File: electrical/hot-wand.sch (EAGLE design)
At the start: 203 parts, among them IC1 12V R-78K12-2.0, IC2 3V3 R-78K3.3, Q1 STP19NF20, Q2 IRF510, Q3 BC846B, Q4 SIS862ADN-T1-GE3, Q5 SIS862ADN-T1-GE3, Q6 DMTH64M2LPDWQ-13, Q7 SIS862ADN-T1-GE3, Q8 2N7002K, Q9 G3404, SW1 SW-TACT-SIDE, U1 TPS54560DDA, U2 1EDN8511BXUSA1, U3 STM32F030F4P6, U4 SSD1306-4PIN-0.91N-VERT, U5 INA138, U6 LM74810QDRRRQ1, U7 AP53781, Y1 27.12 MHz 10pF

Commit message: part num update
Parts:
- U3: value STM32F030F4P6 -> STM32F042F6P6
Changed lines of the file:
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@@
 <attribute name="JLC-DNP" value="1"/>
 </part>
-<part name="U3" library="hot-wand" deviceset="STM32F030F4P6" device="">
+<part name="U3" library="hot-wand" deviceset="STM32F030F4P6" device="" value="STM32F042F6P6">
 <attribute name="JLCPARTNUM" value="C2969989"/>
 <attribute name="JLC_ROTATION" value="180"/>

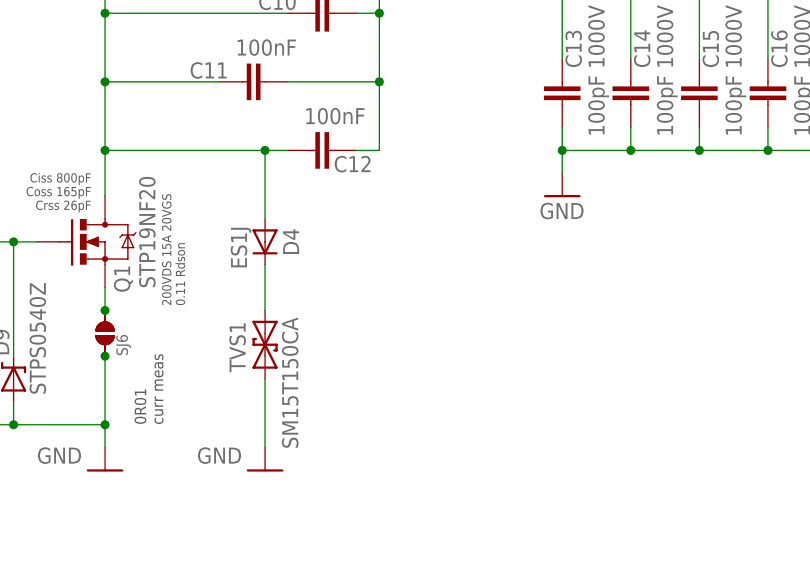
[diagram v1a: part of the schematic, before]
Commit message: lower voltage input limit for lite design
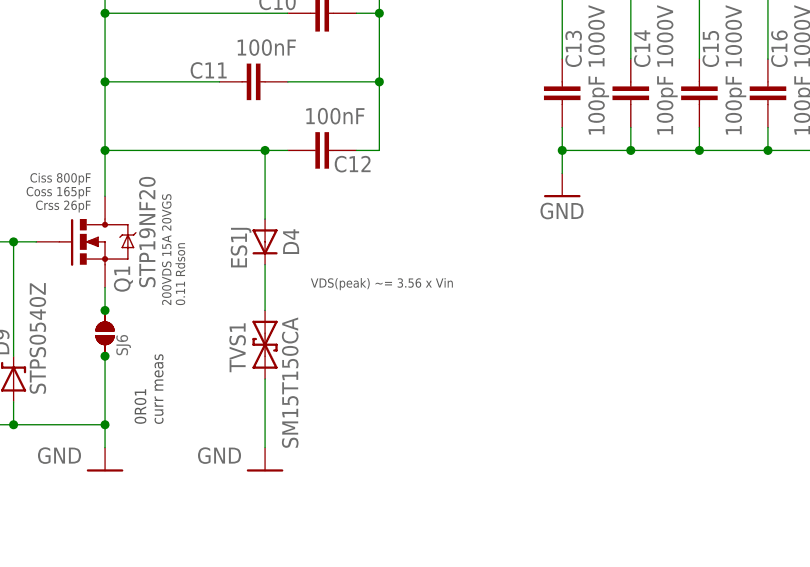
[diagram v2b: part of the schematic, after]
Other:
- note added: "VDS(peak) ~= 3.56 x Vin"
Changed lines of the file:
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@@
 from high battery voltage</text>
 <text x="130.556" y="-596.138" size="1.016" layer="97">50V each</text>
+<text x="81.28" y="-177.8" size="1.016" layer="97">VDS(peak) ~= 3.56 x Vin</text>
 </plain>
 <instances>

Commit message: capacitor footprint improvements
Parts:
- removed FAN2: FAN-TIEDOWN-20MM-V1, hot-wand:FAN-TIEDOWN-20MM-V1
- C2, C4: device hot-wand:CAP_POLPTH4 -> hot-wand:CAP_POLPTH5
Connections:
- net GND: no longer FAN2.1
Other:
- note removed: "MS2006H12D-RSR"
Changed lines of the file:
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@@
 <attribute name="JLCPARTNUM" value="C1613"/>
 </part>
-<part name="C2" library="hot-wand" deviceset="CAP_POL" device="PTH4" value="100uF 50V">
+<part name="C2" library="hot-wand" deviceset="CAP_POL" device="PTH5" value="100uF 50V">
 <attribute name="JLC-DNP" value="1"/>
 <attribute name="PARTNUM" value="EEU-FR1H101B;EEU-FR1J101B"/>
@@
 <attribute name="JLCPARTNUM" value="C21190"/>
 </part>
-<part name="C4" library="hot-wand" deviceset="CAP_POL" device="PTH4" value="100uF 50V">
+<part name="C4" library="hot-wand" deviceset="CAP_POL" device="PTH5" value="100uF 50V">
 <attribute name="JLC-DNP" value="1"/>
 </part>
@@
 <attribute name="PARTNUM" value="MLASU31LBB5106KTNA01;GRT31CR61H106KE01K"/>
 </part>
-<part name="FAN2" library="hot-wand" deviceset="FAN-TIEDOWN" device="-20MM-V1" value="FAN-TIEDOWN-20MM-V1">
-<attribute name="JLC-DNP" value="1"/>
-<attribute name="PARTNUM" value="MS2006H12D-RSR"/>
-</part>
 <part name="PCB2" library="hot-wand" deviceset="PCB-ART-VERSION" device="">
 <attribute name="JLC-DNP" value="1"/>
@@
 <part name="GND61" library="hot-wand" deviceset="GND" device=""/>
 <part name="GND1" library="hot-wand" deviceset="GND" device=""/>
-<part name="GND62" library="hot-wand" deviceset="GND" device=""/>
 <part name="SJ8" library="hot-wand" deviceset="SJ-SMALL" device="-1206-SJ"/>
 <part name="SJ6" library="hot-wand" deviceset="SJ-SMALL" device="-1206-SJ"/>
@@
 <text x="121.158" y="-34.036" size="0.8128" layer="97" rot="R180" align="top-left">FB target 0.8V</text>
 <text x="161.798" y="-14.478" size="0.6096" layer="97" rot="R180" align="top-left">calculations say 13uH minimum</text>
-<text x="289.56" y="-415.544" size="0.8128" layer="97" rot="R180" align="top-left">MS2006H12D-RSR</text>
 <text x="312.42" y="-472.44" size="5.08" layer="97">Fan CTRL</text>
 <text x="312.42" y="-474.98" size="1.778" layer="97">(optional)</text>
@@
 <attribute name="JLCPARTNUM" x="337.82" y="-408.94" size="1.778" layer="96" rot="R270" display="off"/>
 </instance>
-<instance part="FAN2" gate="A" x="271.78" y="-426.72" smashed="yes">
-<attribute name="NAME" x="271.78" y="-429.26" size="1.778" layer="95"/>
-</instance>
 <instance part="PCB2" gate="A" x="322.58" y="-25.4"/>
 <instance part="Q9" gate="G$1" x="327.66" y="-447.04" smashed="yes">
@@
 <attribute name="VALUE" x="307.34" y="-27.94" size="1.778" layer="96"/>
 </instance>
-<instance part="GND62" gate="1" x="292.1" y="-421.64"/>
 <instance part="SJ8" gate="A" x="35.56" y="-223.52"/>
 <instance part="SJ6" gate="A" x="58.42" y="-182.88" rot="R90"/>
@@
 </segment>
 <segment>
-<pinref part="FAN2" gate="A" pin="1"/>
-<pinref part="GND62" gate="1" pin="GND"/>
-</segment>
-<segment>

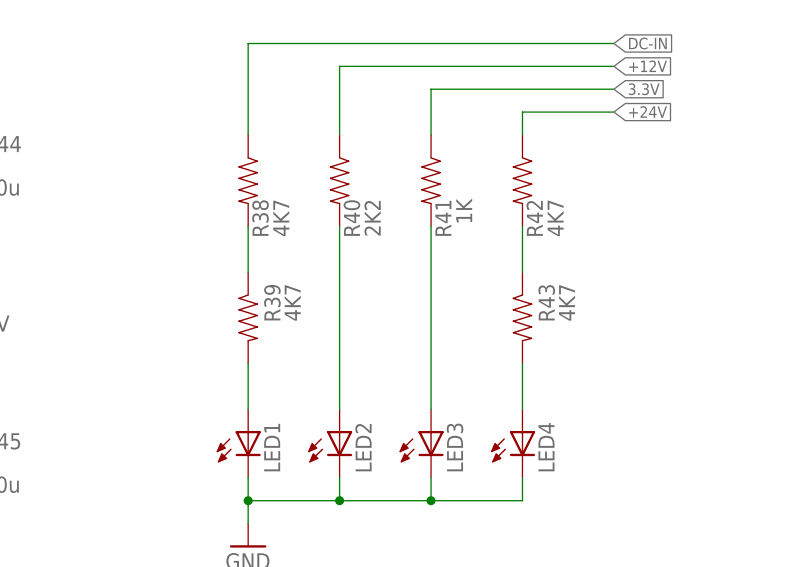
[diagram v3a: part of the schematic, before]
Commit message: inductor pin spacing, capacitor footprint silk, LED resistor changes
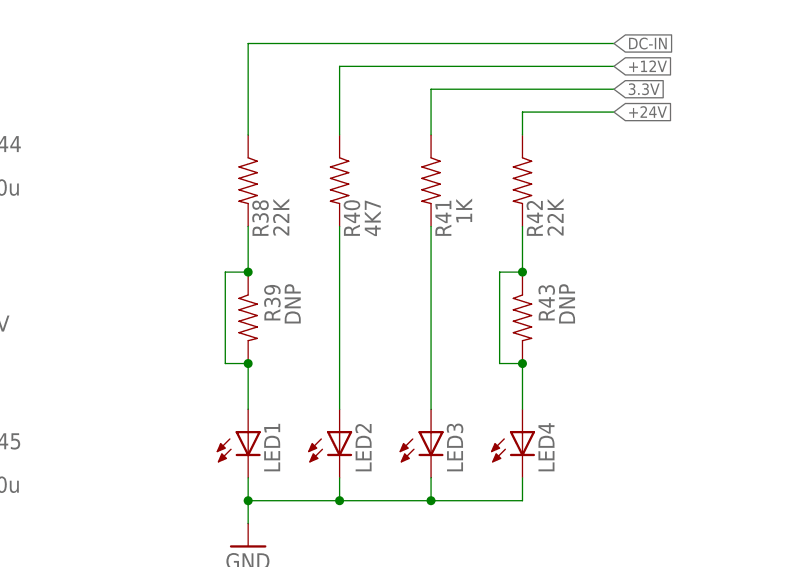
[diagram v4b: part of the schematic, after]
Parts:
- L1: device hot-wand:INDUCTORRADIAL_D12.7_P6.35 -> hot-wand:INDUCTORRADIAL_D12.7_COMBO
- R38, R42: value 4K7 -> 22K; JLCPARTNUM C23162 -> C31850
- R39, R43: value 4K7 -> DNP; DNP (none) -> 1; JLCPARTNUM C23162 -> (none)
- R40: value 2K2 -> 4K7; JLCPARTNUM C4190 -> C23162
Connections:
- removed net N$46: LED1.A, R39.2
- removed net N$64: LED4.A, R43.2
- net N$49: now also LED1.A, R39.2
- net N$62: now also LED4.A, R43.2

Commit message: corrected pot direction
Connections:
- net 3.3V: now also VR2.E; no longer VR2.A
- net BUCK-FB: now also VR1.A; no longer VR1.E
- net N$25: now also VR1.E; no longer VR1.A
- net N$45: now also VR2.A; no longer VR2.E
- net N$50: now also VR4.E; no longer VR4.A
- net N$56: now also VR3.E; no longer VR3.A
- net N$8: now also VR3.A; no longer VR3.E
- net RF-FB-RECTIFIED: now also VR4.A; no longer VR4.E
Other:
- moved on the sheet: VR1, VR4

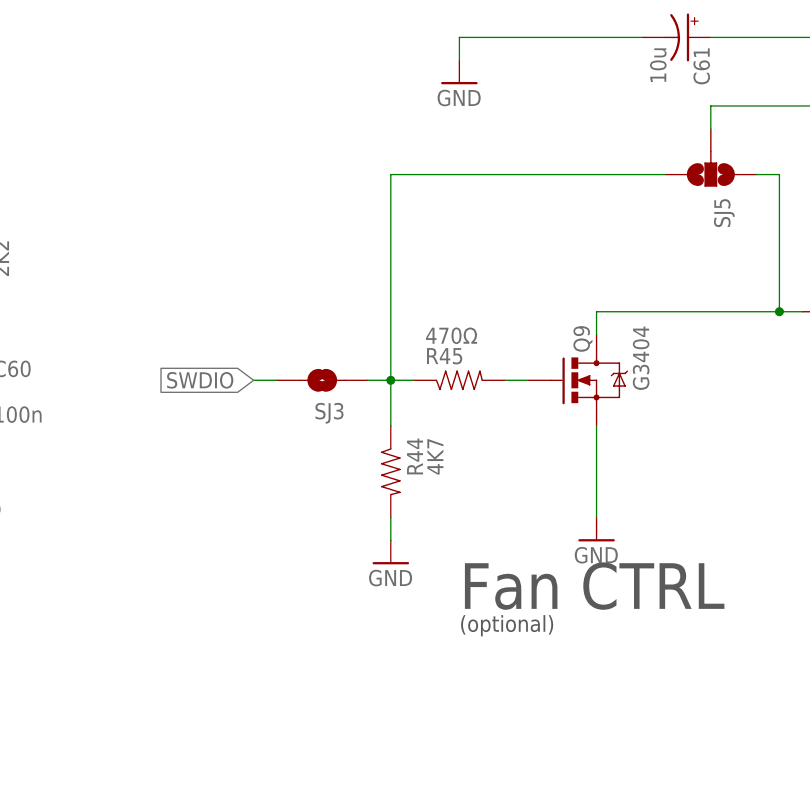
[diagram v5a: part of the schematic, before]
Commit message: renamed nets
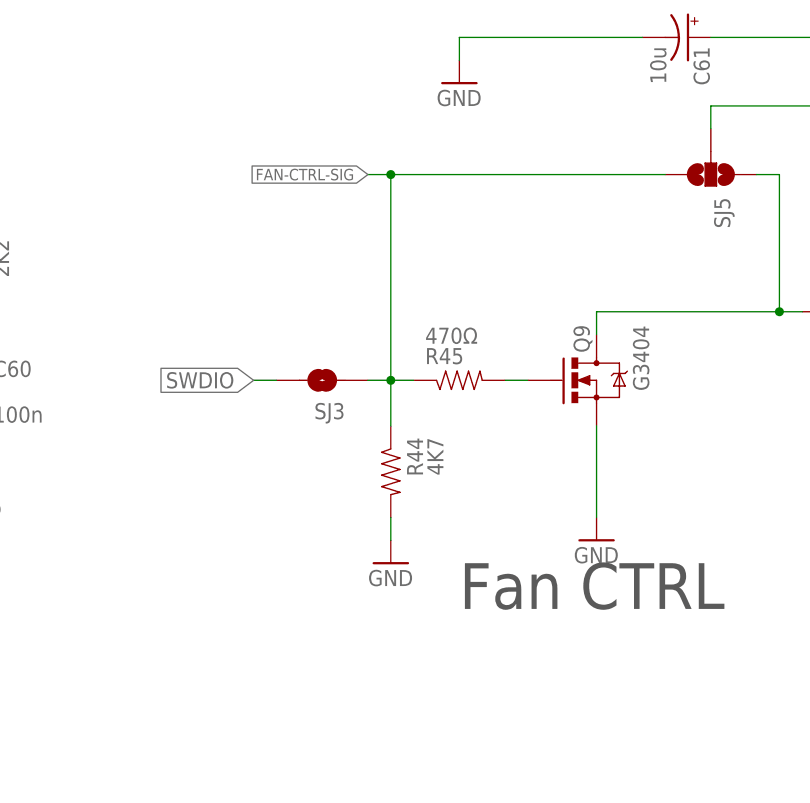
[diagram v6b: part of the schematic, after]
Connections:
- net N$12 renamed RF-FINAL
- net N$13 renamed Q1-VD
- net N$18 renamed Q2-VD
- net N$23 renamed BUCK-SWITCH-NODE
- net N$24 renamed BUCK-1ST-STAGE
- net N$26 renamed MCU-BOOT0
- net N$31 renamed VIN-XT30
- net N$32 renamed U6-EN
- net N$33 renamed MCU-OSC-OUT
- net N$34 renamed MCU-OSC-IN
- net N$36 renamed U7-VGA
- net N$37 renamed U7-VGA-2
- net N$39 renamed USB-VBUS
- net N$41 renamed USB-CC2
- net N$42 renamed U7-VSEL
- net N$44 renamed USB-CC1
- net N$51 renamed FAN-CTRL-SIG
- net N$52 renamed Q9-VD
- net N$54 renamed U7-ISEL
- net N$56 renamed Q3-VB
- net N$58 renamed 12V-FOR-GATE-DRIVER
- net N$59 renamed Q1-VS
- net N$66 renamed U6-HGATE
- net N$69 renamed U6-CAP
- net N$70 renamed U6-DGATE
- net N$71 renamed U6-OV
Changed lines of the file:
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@@
 <text x="161.798" y="-14.478" size="0.6096" layer="97" rot="R180" align="top-left">calculations say 13uH minimum</text>
 <text x="312.42" y="-472.44" size="5.08" layer="97">Fan CTRL</text>
-<text x="312.42" y="-474.98" size="1.778" layer="97">(optional)</text>
 <text x="284.48" y="-320.04" size="1.778" layer="97">debug port</text>
 <text x="78.232" y="-420.37" size="0.8128" layer="97" rot="R180" align="top-left">rated 36V max
@@
 </segment>
 </net>
-<net name="N$12" class="0">
+<net name="RF-FINAL" class="0">
 <segment>
 <pinref part="L6" gate="G$1" pin="2"/>
@@
 </segment>
 </net>
-<net name="N$13" class="0">
+<net name="Q1-VD" class="0">
 <segment>
 <pinref part="C9" gate="G$1" pin="1"/>
@@
 </segment>
 </net>
-<net name="N$18" class="0">
+<net name="Q2-VD" class="0">
 <segment>
 <pinref part="L7" gate="G$1" pin="1"/>
@@
 </segment>
 </net>
-<net name="N$23" class="0">
+<net name="BUCK-SWITCH-NODE" class="0">
 <segment>
 <pinref part="U1" gate="G$1" pin="SW"/>
@@
 </segment>
 </net>
-<net name="N$24" class="0">
+<net name="BUCK-1ST-STAGE" class="0">
 <segment>
 <wire x1="160.02" y1="-20.32" x2="162.56" y2="-20.32" width="0.1524" layer="91"/>
@@
 </segment>
 </net>
-<net name="N$31" class="0">
+<net name="VIN-XT30" class="0">
 <segment>
 <wire x1="76.2" y1="-579.12" x2="73.66" y2="-579.12" width="0.1524" layer="91"/>
@@
 </segment>
 </net>
-<net name="N$36" class="0">
+<net name="U7-VGA" class="0">
 <segment>
 <pinref part="U7" gate="A" pin="VG_A"/>
@@
 </segment>
 </net>
-<net name="N$37" class="0">
+<net name="U7-VGA-2" class="0">
 <segment>
 <pinref part="R30" gate="G$1" pin="1"/>
@@
 </segment>
 </net>
-<net name="N$39" class="0">
+<net name="USB-VBUS" class="0">
 <segment>
 <pinref part="JP2" gate="G$1" pin="VBUS"/>
@@
 </segment>
 </net>
-<net name="N$42" class="0">
+<net name="U7-VSEL" class="0">
 <segment>
 <pinref part="U7" gate="A" pin="VSEL"/>
@@
 </segment>
 </net>
-<net name="N$41" class="0">
+<net name="USB-CC2" class="0">
 <segment>
 <pinref part="JP2" gate="G$1" pin="CC2"/>
@@
 </segment>
 </net>
-<net name="N$44" class="0">
+<net name="USB-CC1" class="0">
 <segment>
 <pinref part="JP2" gate="G$1" pin="CC1"/>
@@
 </segment>
 </net>
-<net name="N$33" class="0">
+<net name="MCU-OSC-OUT" class="0">
 <segment>
 <pinref part="Y1" gate="G$1" pin="1"/>
@@
 </segment>
 </net>
-<net name="N$34" class="0">
+<net name="MCU-OSC-IN" class="0">
 <segment>
 <pinref part="U3" gate="G$1" pin="PF0/OSC_IN"/>
@@
 </segment>
 </net>
-<net name="N$26" class="0">
+<net name="MCU-BOOT0" class="0">
 <segment>
 <pinref part="U3" gate="G$1" pin="BOOT0"/>
@@
 </segment>
 </net>
-<net name="N$52" class="0">
+<net name="Q9-VD" class="0">
 <segment>
 <pinref part="Q9" gate="G$1" pin="D"/>
@@
 </segment>
 </net>
-<net name="N$51" class="0">
+<net name="FAN-CTRL-SIG" class="0">
 <segment>
 <pinref part="R44" gate="G$1" pin="1"/>
@@
 <pinref part="SJ5" gate="G$1" pin="3"/>
 <wire x1="335.28" y1="-424.18" x2="304.8" y2="-424.18" width="0.1524" layer="91"/>
+<wire x1="304.8" y1="-424.18" x2="302.26" y2="-424.18" width="0.1524" layer="91"/>
+<junction x="304.8" y="-424.18"/>
+<label x="302.26" y="-424.18" size="1.27" layer="95" rot="R180" xref="yes"/>
 </segment>
 </net>
@@
 </segment>
 </net>
-<net name="N$56" class="0">
+<net name="Q3-VB" class="0">
 <segment>
 <wire x1="307.34" y1="-264.16" x2="307.34" y2="-256.54" width="0.1524" layer="91"/>
@@
 </segment>
 </net>
-<net name="N$58" class="0">
+<net name="12V-FOR-GATE-DRIVER" class="0">
 <segment>
 <pinref part="U2" gate="G$1" pin="VDD"/>
@@
 </segment>
 </net>
-<net name="N$59" class="0">
+<net name="Q1-VS" class="0">
 <segment>
 <pinref part="Q1" gate="G$1" pin="S"/>
@@
 </segment>
 </net>
-<net name="N$54" class="0">
+<net name="U7-ISEL" class="0">
 <segment>
 <pinref part="U7" gate="A" pin="ISEL"/>
@@
 </segment>
 </net>
-<net name="N$32" class="0">
+<net name="U6-EN" class="0">
 <segment>
 <pinref part="Q8" gate="G$1" pin="D"/>
@@
 </segment>
 </net>
-<net name="N$66" class="0">
+<net name="U6-HGATE" class="0">
 <segment>
 <pinref part="U6" gate="A" pin="HGATE"/>
@@
 </segment>
 </net>
-<net name="N$69" class="0">
+<net name="U6-CAP" class="0">
 <segment>
 <pinref part="U6" gate="A" pin="CAP"/>
@@
 </segment>
 </net>
-<net name="N$70" class="0">
+<net name="U6-DGATE" class="0">
 <segment>
 <pinref part="U6" gate="A" pin="DGATE"/>
@@
 </segment>
 </net>
-<net name="N$71" class="0">
+<net name="U6-OV" class="0">
 <segment>
 <pinref part="R53" gate="G$1" pin="1"/>

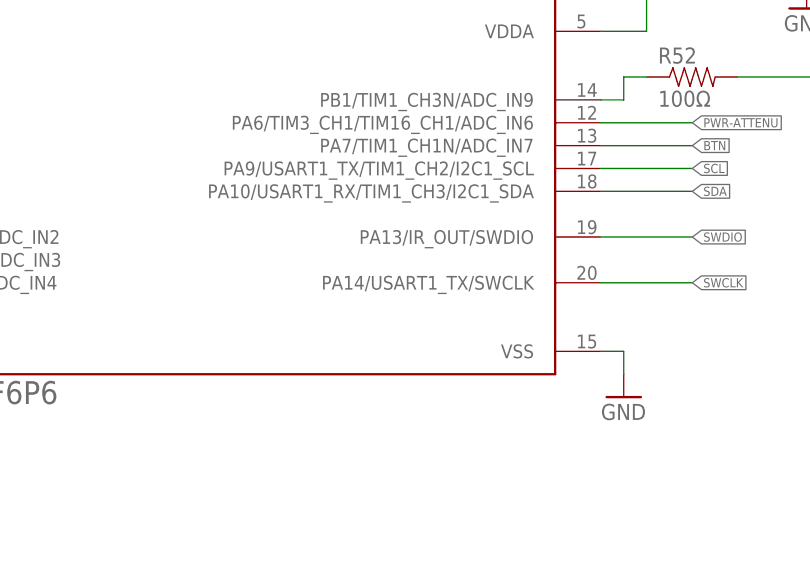
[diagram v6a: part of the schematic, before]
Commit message: inductor footprint larger pads, stm32f042 uses USART2 for debug
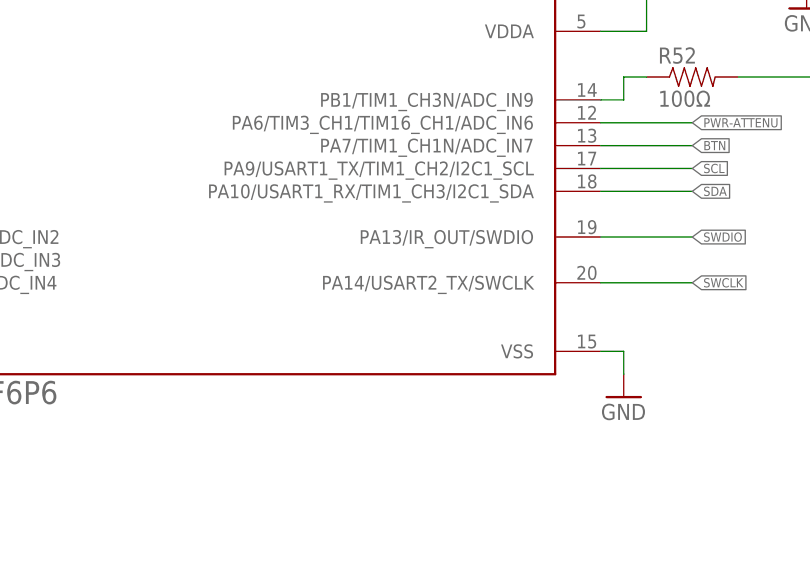
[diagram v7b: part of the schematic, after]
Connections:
- net SWCLK: now also U3.PA14/USART2_TX/SWCLK; no longer U3.PA14/USART1_TX/SWCLK
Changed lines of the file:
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@@
 <net name="SWCLK" class="0">
 <segment>
-<pinref part="U3" gate="G$1" pin="PA14/USART1_TX/SWCLK"/>
+<pinref part="U3" gate="G$1" pin="PA14/USART2_TX/SWCLK"/>
 <wire x1="167.64" y1="-353.06" x2="177.8" y2="-353.06" width="0.1524" layer="91"/>
 <label x="177.8" y="-353.06" size="1.016" layer="95" xref="yes"/>

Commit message: pcb assembly problems being addressed
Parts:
- C10, C11, C12, C13, C14, C15, C16, C17, C18, C19, C20, C21, C22, C23, C24, C25, C26, C27, C28, C29, C30, C31, C32, C33, C37, C38, C39, C40, C9: device hot-wand:CAP0805 -> hot-wand:CAP0805-L
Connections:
- removed net N$45: R19.1, R20.1, VR2.A, VR2.S
- removed net N$8: R22.1, VR3.A
- net 3.3V: now also R19.1, R20.1, VR2.A, VR2.S
- net Q3-VB: now also R22.1, VR3.A
